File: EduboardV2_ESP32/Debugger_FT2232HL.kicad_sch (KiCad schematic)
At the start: 30 parts, among them U2 FT2232HL, U3 93CxxC, Y1 12MHz

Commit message: work on debug chip
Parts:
- added C10, C11, C12, C13, C14, C15, C16: 100n, symbol Device:C
- added D4, D5, D6, D7, D8, D9: LED, symbol Device:LED
- added R13, R14, R17, R18, R19, R20: 2k2, symbol Device:R
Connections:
- net +1V8: now also C10.2, C11.2, C12.2
- net +3V3: now also C13.2, C14.2, C15.2, C16.2, R13.1, R14.1
- net GND: now also C10.1, C11.1, C12.1, C13.1, C14.1, C15.1, C16.1, D4.1 (K), D5.1 (K), D6.1 (K), D7.1 (K)
- net TCK: now reaches U2.16 (ADBUS0)
- net TDI: now reaches U2.17 (ADBUS1)
- net TDO: now reaches U2.18 (ADBUS2)
- net TMS: now reaches U2.19 (ADBUS3)
- net nTRST: now reaches U2.22 (ADBUS5)
- net at U2.30 (ACBUS4): now also R17.2
- net at U2.32 (ACBUS5): now also R18.2
- net at U2.33 (ACBUS6): now also R19.2
- net at U2.34 (ACBUS7): now also R20.2
- net nSUSPEND: now reaches U2.36 (~{SUSPEND})
- net TXD: now reaches U2.38 (BDBUS0)
- net RXD: now reaches U2.39 (BDBUS1)
- net nRTS: now reaches U2.40 (BDBUS2)
- net nCTS: now reaches U2.41 (BDBUS3)
- net nDTR: now reaches U2.43 (BDBUS4)
- net nDSR: now reaches U2.44 (BDBUS5)
- net nDCD: now reaches U2.45 (BDBUS6)
- net nRI: now reaches U2.46 (BDBUS7)
- net TXDEN: now reaches U2.48 (BCBUS0)
- net at U2.54 (BCBUS3): now also D8.1 (K)
- net at U2.55 (BCBUS4): now also D9.1 (K)
- net nPWRSAV: now reaches U2.59 (BCBUS7)
- net nPWREN: now reaches U2.60 (~{PWREN})
- new net: D9.2 (A), R14.2
- new net: D4.2 (A), R20.1
- new net: D8.2 (A), R13.2
- new net: D6.2 (A), R18.1
- new net: D5.2 (A), R19.1
- new net: D7.2 (A), R17.1
- no-connect marks 2 -> 9
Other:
- moved on the sheet: D1, D2, D3, R6, R7, USBC1

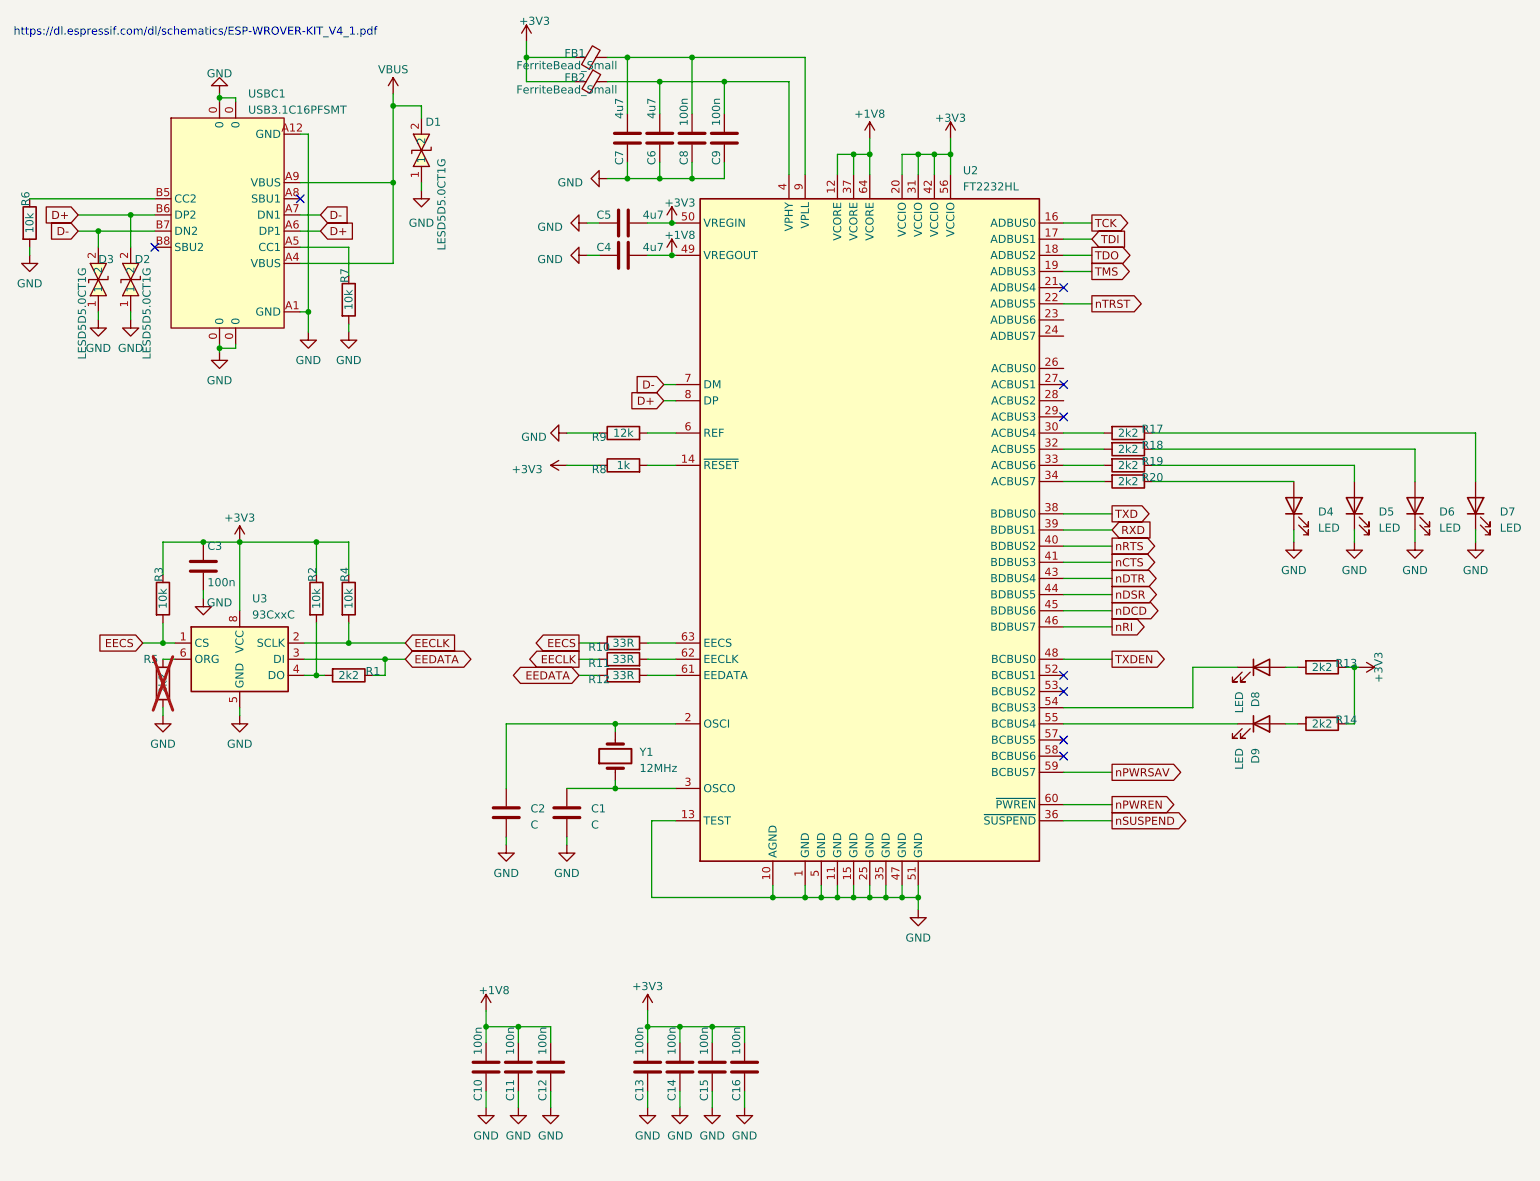
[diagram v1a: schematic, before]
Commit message: finalize ft2232 design, prepare esp pins, work on mpcie pinout
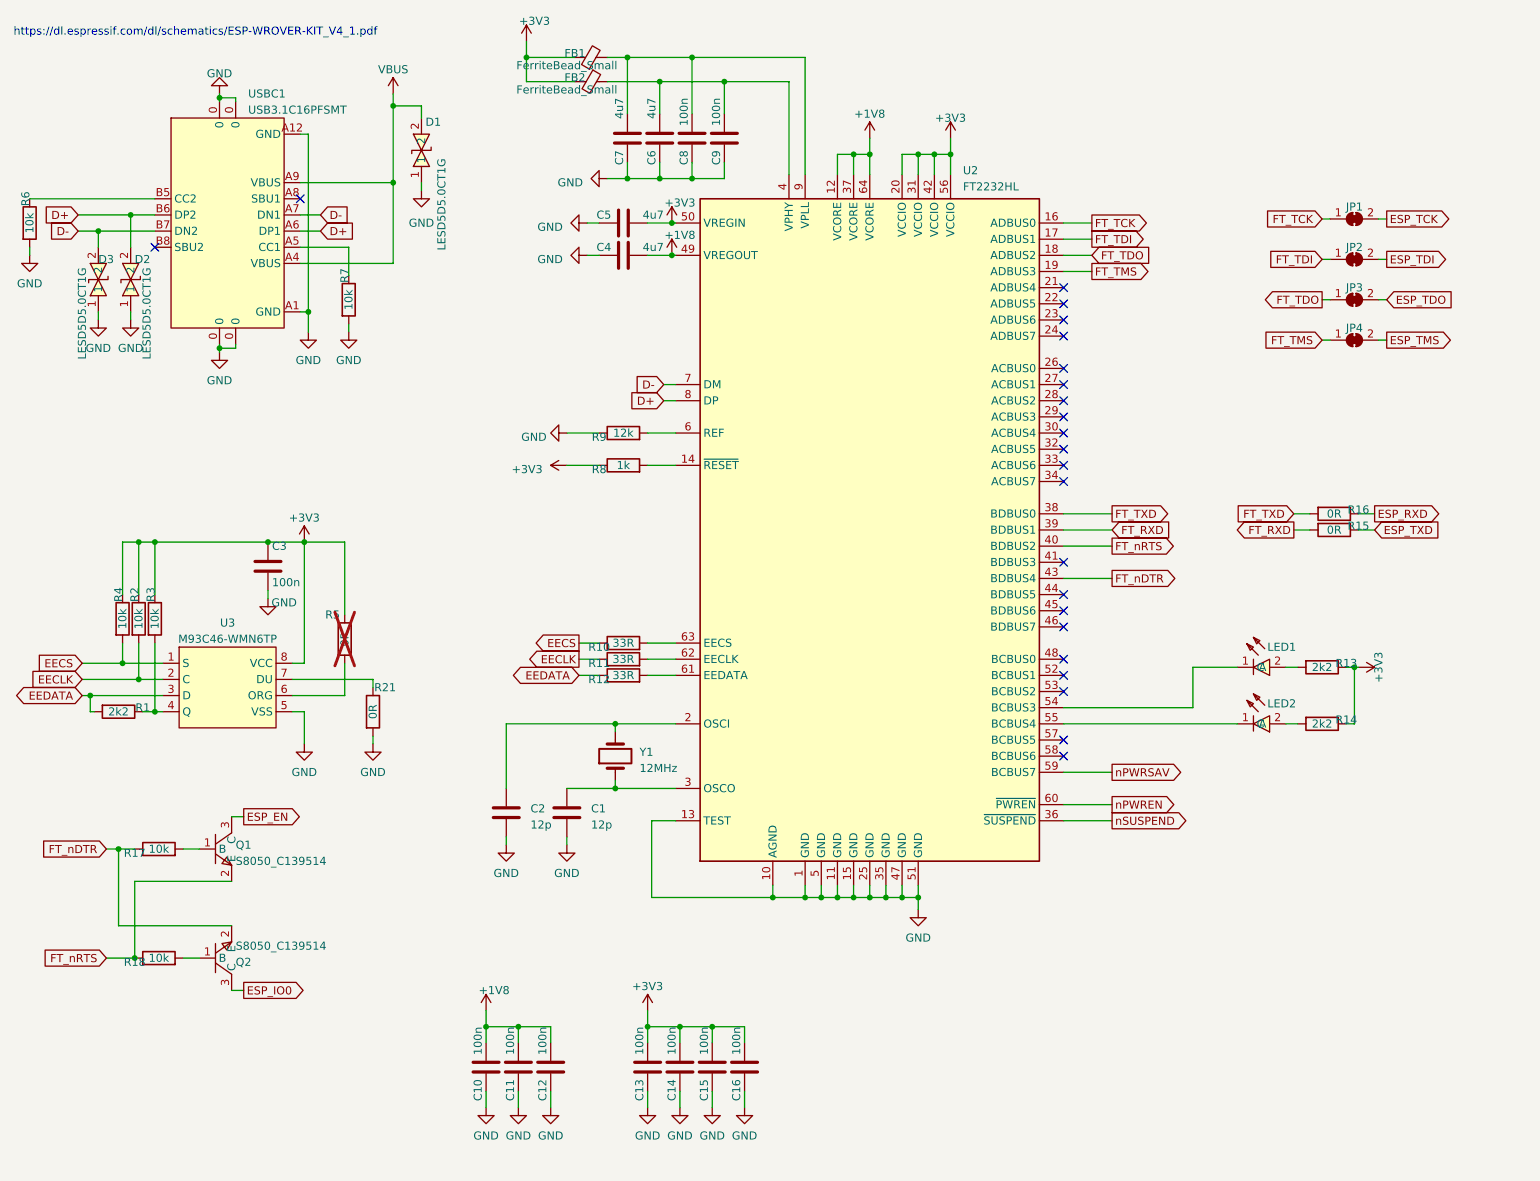
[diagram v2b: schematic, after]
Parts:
- removed D4, D5, D6, D7, D8, D9: LED, symbol Device:LED
- removed R19, R20: 2k2, symbol Device:R
- removed U3: 93CxxC, symbol Memory_EEPROM:93CxxC
- added JP1, JP2, JP3, JP4: SolderJumper_2_Bridged, Jumper:SolderJumper-2_P1.3mm_Bridged_RoundedPad1.0x1.5mm, symbol Jumper:SolderJumper_2_Bridged
- added LED1, LED2: 19-217/BHC-ZL1M2RY/3T, JLCPCB:LED0603-RD, symbol JLCPCB:19-217_BHC-ZL1M2RY_3T
- added Q1, Q2: S8050_C139514, JLCPCB:SOT-23-3_L2.9-W1.3-P1.90-LS2.4-BR, symbol JLCPCB:S8050_C139514
- added R15, R16, R21: 0R, symbol Device:R
- added U3: M93C46-WMN6TP, SOIC-8_L4.9-W3.9-P1.27-LS6.0-BL, symbol JLCPCB:M93C46-WMN6TP
- C1, C2: value C -> 12p
- D1, D2, D3: footprint SOD-523_L1.2-W0.8-LS1.6-BI -> JLCPCB:SOD-523_L1.2-W0.8-LS1.6-BI
- R17, R18: value 2k2 -> 10k
- R5: value 2k2 -> 0R
- USBC1: footprint USB-C-SMD_TYPE-C-USB-17 -> JLCPCB:USB-C-SMD_TYPE-C-USB-17
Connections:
- net nDTR is gone; now on net FT_nDTR: U2.43 (BDBUS4)
- net nRTS is gone; now on net FT_nRTS: U2.40 (BDBUS2)
- net +3V3: now also R5.1, U3.8 (VCC)
- net EECLK: now also R2.2, U3.2 (C); no longer R4.2
- net EECS: now also R4.2, U3.1 (S); no longer R3.2
- net EEDATA: now also R1.2, U3.3 (D); no longer R1.1
- net GND: now also R21.2, U3.5 (VSS); no longer R5.2
- net at U2.30 (ACBUS4): no longer R17.2
- net at U2.32 (ACBUS5): no longer R18.2
- net at U2.54 (BCBUS3): now also LED1.1 (C)
- net at U2.55 (BCBUS4): now also LED2.1 (C)
- net at R14.2: now also LED2.2 (A)
- net at R13.2: now also LED1.2 (A)
- net FT_nRTS: now reaches R18.1
- net FT_nRTS: now also Q1.2 (E)
- net FT_nDTR: now reaches R17.1
- net FT_nDTR: now also Q2.2 (E)
- net RXD renamed FT_RXD
- net FT_RXD: now also R15.2
- net TCK renamed FT_TCK
- net FT_TCK: now also JP1.1 (A)
- net TDI renamed FT_TDI
- net FT_TDI: now also JP2.1 (A)
- net TDO renamed FT_TDO
- net FT_TDO: now also JP3.1 (A)
- net TMS renamed FT_TMS
- net FT_TMS: now also JP4.1 (A)
- net TXD renamed FT_TXD
- net FT_TXD: now also R16.2
- net TXDEN: no longer names the net of U2.48 (BCBUS0)
- net nCTS: no longer names the net of U2.41 (BDBUS3)
- net nDCD: no longer names the net of U2.45 (BDBUS6)
- net nDSR: no longer names the net of U2.44 (BDBUS5)
- net nRI: no longer names the net of U2.46 (BDBUS7)
- net nTRST: no longer names the net of U2.22 (ADBUS5)
- new net: R21.1, U3.7 (DU)
- new net: Q2.1 (B), R18.2
- new net: Q1.1 (B), R17.2
- new net: R1.1, R3.2, U3.4 (Q)
- new net: R5.2, U3.6 (ORG)
- new net ESP_EN: Q1.3 (C)
- new net ESP_IO0: Q2.3 (C)
- new net ESP_RXD: R16.1
- new net ESP_TCK: JP1.2 (B)
- new net ESP_TDI: JP2.2 (B)
- new net ESP_TDO: JP3.2 (B)
- new net ESP_TMS: JP4.2 (B)
- new net ESP_TXD: R15.1
- no-connect marks 9 -> 23
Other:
- moved on the sheet: C3, R1, R2, R3, R4, R5

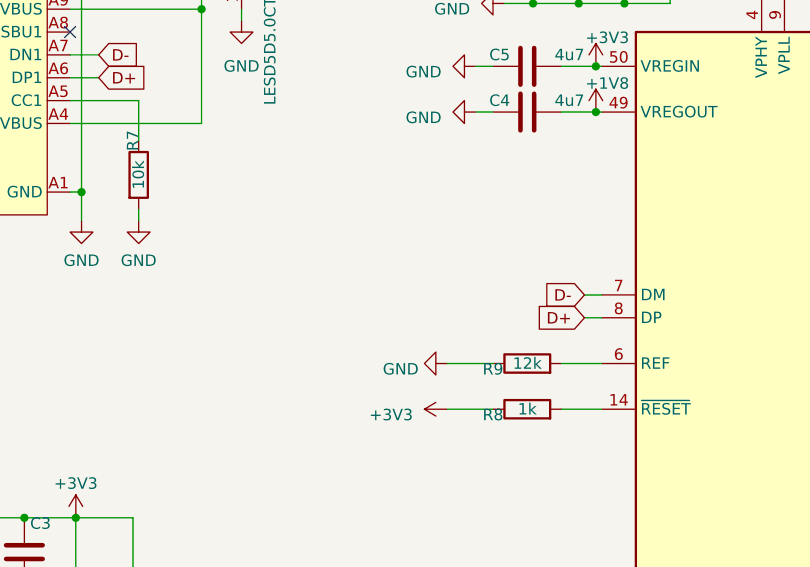
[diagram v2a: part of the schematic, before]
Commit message: add Portexpander, connect mPCIE
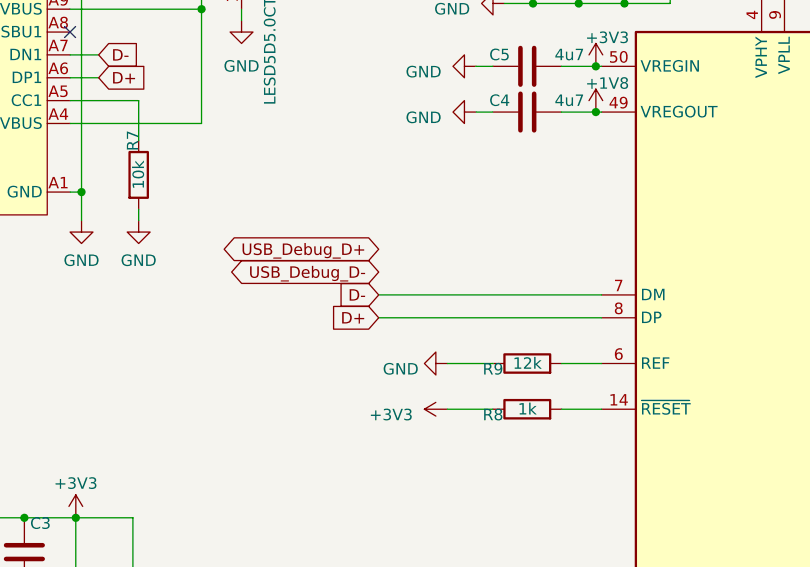
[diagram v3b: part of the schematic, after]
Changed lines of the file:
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@@
     (stroke (width 0) (type default))
   )
-  (wire (pts (xy 116.84 70.485) (xy 118.745 70.485))
+  (wire (pts (xy 93.98 70.485) (xy 118.745 70.485))
     (stroke (width 0) (type default))
   )
@@
     (stroke (width 0) (type default))
   )
-  (wire (pts (xy 116.84 73.025) (xy 118.745 73.025))
+  (wire (pts (xy 93.98 73.025) (xy 118.745 73.025))
     (stroke (width 0) (type default))
   )
@@
     )
   )
-  (global_label "D-" (shape input) (at 116.84 70.485 180) (fields_autoplaced)
-    (effects (font (size 1.27 1.27)) (justify right))
-    (property "Intersheetrefs" "${INTERSHEET_REFS}" (at 111.0918 70.485 0)
+  (global_label "D-" (shape input) (at 93.98 70.485 180) (fields_autoplaced)
+    (effects (font (size 1.27 1.27)) (justify right))
+    (property "Intersheetrefs" "${INTERSHEET_REFS}" (at 88.2318 70.485 0)
       (effects (font (size 1.27 1.27)) (justify right) hide)
     )
@@
     )
   )
+  (global_label "USB_Debug_D-" (shape bidirectional) (at 93.98 67.945 180) (fields_autoplaced)
+    (effects (font (size 1.27 1.27)) (justify right))
+    (property "Intersheetrefs" "${INTERSHEET_REFS}" (at 75.5697 67.945 0)
+      (effects (font (size 1.27 1.27)) (justify right) hide)
+    )
+  )
   (global_label "FT_nDTR" (shape input) (at 29.21 143.51 180) (fields_autoplaced)
     (effects (font (size 1.27 1.27)) (justify right))
@@
     )
   )
+  (global_label "USB_Debug_D+" (shape bidirectional) (at 93.98 65.405 180) (fields_autoplaced)
+    (effects (font (size 1.27 1.27)) (justify right))
+    (property "Intersheetrefs" "${INTERSHEET_REFS}" (at 75.5697 65.405 0)
+      (effects (font (size 1.27 1.27)) (justify right) hide)
+    )
+  )
   (global_label "D+" (shape input) (at 62.865 46.355 0) (fields_autoplaced)
     (effects (font (size 1.27 1.27)) (justify left))
@@
     )
   )
-  (global_label "D+" (shape input) (at 116.84 73.025 180) (fields_autoplaced)
-    (effects (font (size 1.27 1.27)) (justify right))
-    (property "Intersheetrefs" "${INTERSHEET_REFS}" (at 111.0918 73.025 0)
-      (effects (font (size 1.27 1.27)) (justify right) hide)
-    )
+  (global_label "D+" (shape input) (at 93.98 73.025 180) (fields_autoplaced)
+    (effects (font (size 1.27 1.27)) (justify right))
+    (property "Intersheetrefs" "${INTERSHEET_REFS}" (at 88.2318 73.025 0)
+      (effects (font (size 1.27 1.27)) (justify right) hide)
+    )

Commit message: all parts placed. descision about usb-debug line to be made...
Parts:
- removed Y1: 12MHz, symbol Device:Crystal
- added Y2: 12MHz, Crystal:Crystal_SMD_3225-4Pin_3.2x2.5mm, symbol Device:Crystal_GND24
- C1, C10, C11, C12, C13, C14, C15, C16, C2, C3, C8, C9: footprint (none) -> Capacitor_SMD:C_0603_1608Metric
- C4, C5, C6, C7: footprint (none) -> Capacitor_SMD:C_0805_2012Metric
- D1, D2, D3: JLCPCB Part # (none) -> C383211
- FB1, FB2: footprint (none) -> Inductor_SMD:L_0805_2012Metric; JLCPCB Part # (none) -> C44838
- LED1, LED2: JLCPCB Part # (none) -> C72041
- Q1, Q2: JLCPCB Part # (none) -> C139514
- R1, R10, R11, R12, R13, R14, R15, R16, R17, R18, R2, R21, R3, R4, R5, R6, R7, R8, R9: footprint (none) -> Resistor_SMD:R_0603_1608Metric
- U2: LCSC Part (none) -> C27882
- U3: footprint SOIC-8_L4.9-W3.9-P1.27-LS6.0-BL -> JLCPCB:SOIC-8_L4.9-W3.9-P1.27-LS6.0-BL; JLCPCB Part # (none) -> C7565
- USBC1: JLCPCB Part # (none) -> C167321
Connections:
- net GND: now also Y2.2, Y2.4
- net at C2.1, U2.2 (OSCI): now also Y2.3
- net at C1.1, U2.3 (OSCO): now also Y2.1
